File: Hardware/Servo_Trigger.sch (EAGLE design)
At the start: 19 parts, among them Q1 16MHz, U1 ATTINY84

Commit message: PCB Work in progress
Routed board, set up basic jumpers.
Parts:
- added R5, R6: 10k, SparkFun-Passives:RESISTOR0402-RES
- added SJ1, SJ2: N.O., SparkFun-Passives:JUMPER-PAD-2-NOYES_SILK
- JP1, JP3: value M02PTH -> M021X02_NO_SILK; device SparkFun-Connectors:M02PTH -> SparkFun-Connectors:M021X02_NO_SILK
- JP2: device SparkFun-Connectors:M03PTH -> SparkFun-Connectors:M031X03_NO_SILK
- R1, R2, R3: value TRIMPOTRES-11156 -> 10k
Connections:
- new net MODESEL: R5.1, SJ1.2, U1.(PCINT10/INT0/OC0A/CKOUT)PB2
- new net POLSEL: R6.1, SJ2.2, U1.(PCINT2/AIN1/ADC2)PA2
- net GND: now also SJ1.1, SJ2.1
- net VCC: now also R5.2, R6.2
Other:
- note added: "Mode Configuration"
- note added: "Polarity Configuration"
- note added: "Pulled up internally in processor Datasheet says Rup is in the 20K to 50K range."
- note added: "SJ1 sets mode -Open, default, is monostable (one-shot) mode. When input trips, servo will cylce from A to B, then return to A. It will always do the full cycle. -Closed is bistable mode. While input is de-asserted, servo sits at A. While input is asserted, it goes to B, returning to A when input is deasserted. If servo takes longer to travel then the input is held, cycle will be incomplete"
- note added: "SJ2 sets input polarity -Open (default) is active high, pulled up internally. Intended for use with a normally-open switch or active-high logic. -Closed is for normally closed switches, or active low-logic,"

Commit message: PCB updates
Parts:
- JP2: value (none) -> SERVO-OUT
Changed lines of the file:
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@@
 <setting verticaltext="up"/>
 </settings>
-<grid distance="0.1" unitdist="inch" unit="inch" style="lines" multiple="1" display="no" altdistance="0.01" altunitdist="inch" altunit="inch"/>
+<grid distance="0.1" unitdist="inch" unit="inch" style="lines" multiple="1" display="yes" altdistance="0.01" altunitdist="inch" altunit="inch"/>
 <layers>
 <layer number="1" name="Top" color="4" fill="1" visible="no" active="no"/>
@@
 <part name="SUPPLY8" library="SparkFun-Aesthetics" deviceset="VCC" device=""/>
 <part name="JP1" library="SparkFun-Connectors" deviceset="M02" device="1X02_NO_SILK" value="M021X02_NO_SILK"/>
-<part name="JP2" library="SparkFun-Connectors" deviceset="M03" device="1X03_NO_SILK"/>
+<part name="JP2" library="SparkFun-Connectors" deviceset="M03" device="1X03_NO_SILK" value="SERVO-OUT"/>
 <part name="GND4" library="SparkFun-Aesthetics" deviceset="GND" device=""/>
 <part name="GND5" library="SparkFun-Aesthetics" deviceset="GND" device=""/>
@@
 <wire x1="7.62" y1="25.4" x2="12.7" y2="25.4" width="0.1524" layer="91"/>
 <label x="12.7" y="25.4" size="1.27" layer="95" xref="yes"/>
+<junction x="7.62" y="25.4"/>
 </segment>
 </net>
@@
 <wire x1="83.82" y1="25.4" x2="88.9" y2="25.4" width="0.1524" layer="91"/>
 <label x="88.9" y="25.4" size="1.27" layer="95" xref="yes"/>
-</segment>
-</net>
+<junction x="83.82" y="25.4"/>
+</segment>
+</net>

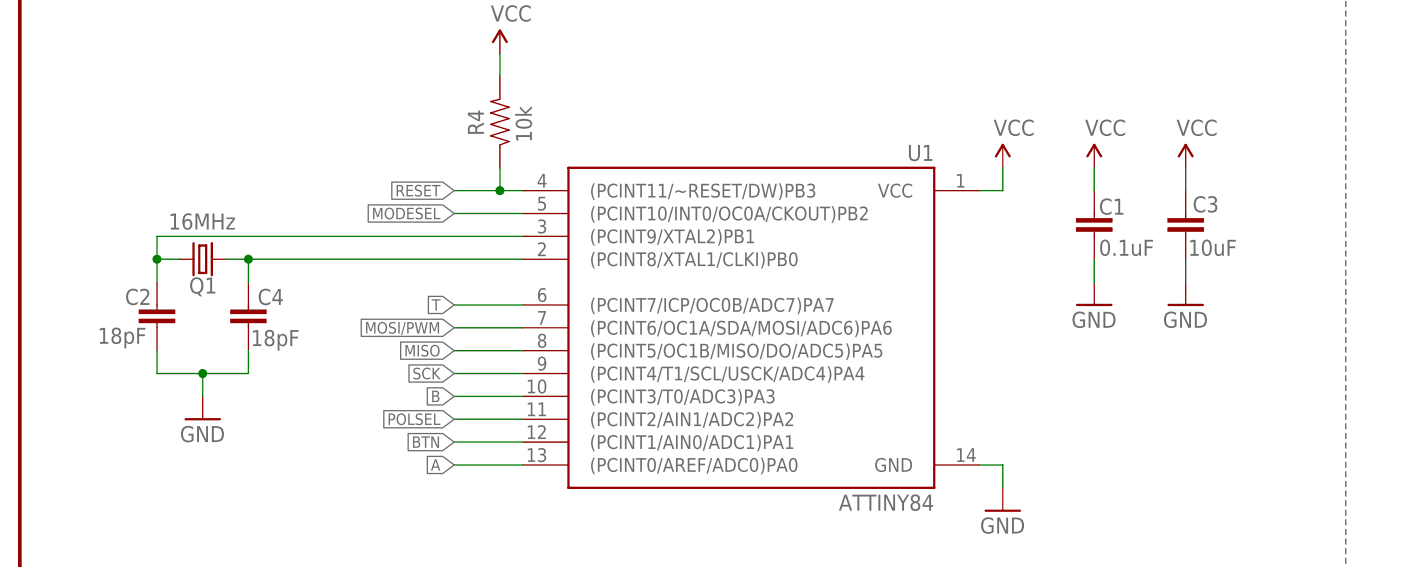
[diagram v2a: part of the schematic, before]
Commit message: Updating parts
I'd cut & pasted the tiny programmer, which used outdated parts.

Updated to 0603 resistors & caps, using resonator instead of crystal,
etc.
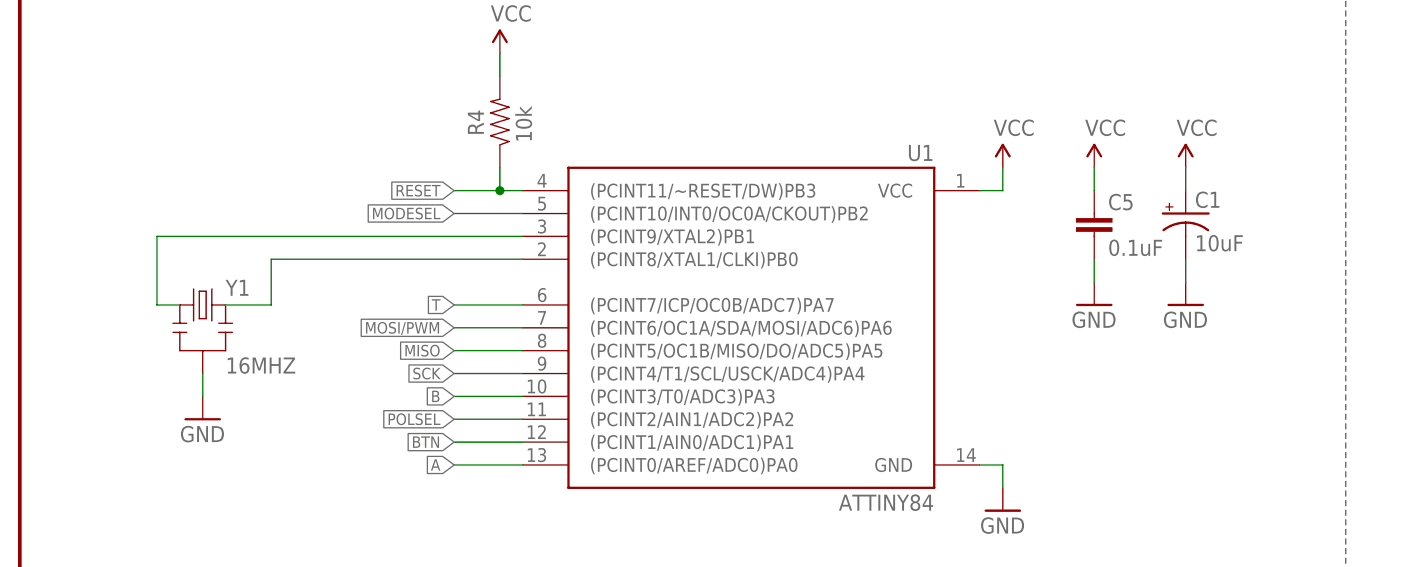
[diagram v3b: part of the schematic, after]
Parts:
- removed C2, C4: 18pF, SparkFun-Passives:CAP0402-CAP
- removed C3: 10uF, SparkFun-Passives:CAP0402-CAP
- removed Q1: 16MHz, SparkFun-FreqCtrl:CRYSTAL5X3
- added C5: 0.1uF, SparkFun-Capacitors:0.1UF-25V(+80/-20%)(0603)
- added Y1: 16MHZ, SparkFun-FreqCtrl:RESONATOR16MHZ
- C1: value 0.1uF -> 10uF; device SparkFun-Passives:CAP0402-CAP -> SparkFun-Capacitors:10UF-16V-10%(TANT)
- R4, R5, R6: device SparkFun-Passives:RESISTOR0402-RES -> SparkFun-Resistors:10KOHM1/10W1%(0603)0603
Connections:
- net GND: now also C1.-, C5.2, Y1.2; no longer C1.2, C2.2, C3.2, C4.2
- net N$3: now also Y1.1; no longer C2.1, Q1.2
- net N$4: now also Y1.3; no longer C4.1, Q1.1
- net VCC: now also C1.+, C5.1; no longer C1.1, C3.1

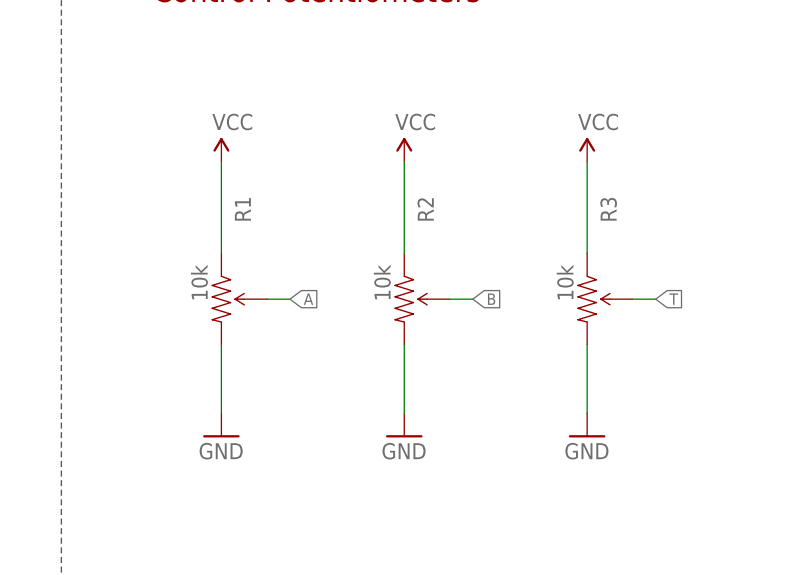
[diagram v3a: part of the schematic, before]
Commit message: More WIP.
Added one-shot FSM.
Cleaned up gratuitous magic constants.
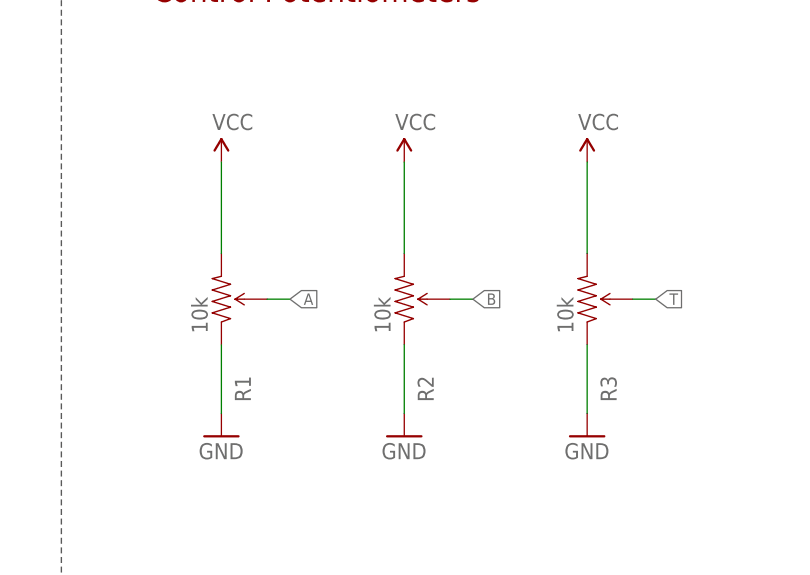
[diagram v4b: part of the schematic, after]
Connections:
- net GND: now also R1.CCW, R2.CCW, R3.CCW; no longer R1.CW, R2.CW, R3.CW
- net VCC: now also R1.CW, R2.CW, R3.CW; no longer R1.CCW, R2.CCW, R3.CCW
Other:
- moved on the sheet: R1, R2, R3
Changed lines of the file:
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@@
 <setting verticaltext="up"/>
 </settings>
-<grid distance="0.1" unitdist="inch" unit="inch" style="lines" multiple="1" display="yes" altdistance="0.01" altunitdist="inch" altunit="inch"/>
+<grid distance="0.1" unitdist="inch" unit="inch" style="lines" multiple="1" display="no" altdistance="0.01" altunitdist="inch" altunit="inch"/>
 <layers>
 <layer number="1" name="Top" color="4" fill="1" visible="no" active="no"/>
@@
 <instance part="GND14" gate="1" x="119.38" y="83.82"/>
 <instance part="GND15" gate="1" x="129.54" y="83.82"/>
-<instance part="R1" gate="R?" x="165.1" y="93.98" rot="R270"/>
-<instance part="R2" gate="R?" x="185.42" y="93.98" rot="R270"/>
-<instance part="R3" gate="R?" x="205.74" y="93.98" rot="R270"/>
+<instance part="R1" gate="R?" x="165.1" y="93.98" rot="MR90"/>
+<instance part="R2" gate="R?" x="185.42" y="93.98" rot="MR90"/>
+<instance part="R3" gate="R?" x="205.74" y="93.98" rot="MR90"/>
 <instance part="GND1" gate="1" x="205.74" y="78.74"/>
 <instance part="GND2" gate="1" x="185.42" y="78.74"/>
@@
 </segment>
 <segment>
-<pinref part="SUPPLY8" gate="G$1" pin="VCC"/>
-<pinref part="R3" gate="R?" pin="CCW"/>
-<wire x1="205.74" y1="109.22" x2="205.74" y2="99.06" width="0.1524" layer="91"/>
-</segment>
-<segment>
-<pinref part="SUPPLY6" gate="G$1" pin="VCC"/>
-<pinref part="R2" gate="R?" pin="CCW"/>
-<wire x1="185.42" y1="109.22" x2="185.42" y2="99.06" width="0.1524" layer="91"/>
-</segment>
-<segment>
-<pinref part="SUPPLY5" gate="G$1" pin="VCC"/>
-<pinref part="R1" gate="R?" pin="CCW"/>
-<wire x1="165.1" y1="109.22" x2="165.1" y2="99.06" width="0.1524" layer="91"/>
-</segment>
-<segment>
 <pinref part="JP2" gate="G$1" pin="2"/>
 <pinref part="SUPPLY9" gate="G$1" pin="VCC"/>
@@
 <pinref part="SUPPLY12" gate="G$1" pin="VCC"/>
 </segment>
+<segment>
+<pinref part="R1" gate="R?" pin="CW"/>
+<pinref part="SUPPLY5" gate="G$1" pin="VCC"/>
+<wire x1="165.1" y1="99.06" x2="165.1" y2="109.22" width="0.2032" layer="91"/>
+</segment>
+<segment>
+<pinref part="R3" gate="R?" pin="CW"/>
+<pinref part="SUPPLY8" gate="G$1" pin="VCC"/>
+<wire x1="205.74" y1="99.06" x2="205.74" y2="109.22" width="0.2032" layer="91"/>
+</segment>
+<segment>
+<pinref part="R2" gate="R?" pin="CW"/>
+<pinref part="SUPPLY6" gate="G$1" pin="VCC"/>
+<wire x1="185.42" y1="99.06" x2="185.42" y2="109.22" width="0.2032" layer="91"/>
+</segment>
 </net>
 <net name="GND" class="0">
@@
 </segment>
 <segment>
-<pinref part="R1" gate="R?" pin="CW"/>
-<pinref part="GND3" gate="1" pin="GND"/>
-<wire x1="165.1" y1="88.9" x2="165.1" y2="81.28" width="0.1524" layer="91"/>
-</segment>
-<segment>
-<pinref part="R2" gate="R?" pin="CW"/>
-<pinref part="GND2" gate="1" pin="GND"/>
-<wire x1="185.42" y1="88.9" x2="185.42" y2="81.28" width="0.1524" layer="91"/>
-</segment>
-<segment>
-<pinref part="R3" gate="R?" pin="CW"/>
-<pinref part="GND1" gate="1" pin="GND"/>
-<wire x1="205.74" y1="88.9" x2="205.74" y2="81.28" width="0.1524" layer="91"/>
-</segment>
-<segment>
 <pinref part="JP2" gate="G$1" pin="1"/>
 <pinref part="GND5" gate="1" pin="GND"/>
@@
 <wire x1="83.82" y1="7.62" x2="83.82" y2="12.7" width="0.1524" layer="91"/>
 </segment>
+<segment>
+<pinref part="R1" gate="R?" pin="CCW"/>
+<pinref part="GND3" gate="1" pin="GND"/>
+<wire x1="165.1" y1="88.9" x2="165.1" y2="81.28" width="0.2032" layer="91"/>
+</segment>
+<segment>
+<pinref part="R3" gate="R?" pin="CCW"/>
+<pinref part="GND1" gate="1" pin="GND"/>
+<wire x1="205.74" y1="88.9" x2="205.74" y2="81.28" width="0.2032" layer="91"/>
+</segment>
+<segment>
+<pinref part="GND2" gate="1" pin="GND"/>
+<pinref part="R2" gate="R?" pin="CCW"/>
+<wire x1="185.42" y1="81.28" x2="185.42" y2="88.9" width="0.2032" layer="91"/>
+</segment>
 </net>
